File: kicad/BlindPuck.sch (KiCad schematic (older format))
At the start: 9 parts, among them Q1 FQP30N06, U1 PK-21N30P-TPQ, U2 DD06AJSA, U3 PK-21N30P-TPQ, U4 FeatherHuzzah, U5 InductiveCoil, U6 MPU-6050

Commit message: replacing the mpu6050
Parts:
- added R?: 1M, symbol R
- added R?: 100, symbol R
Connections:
- net EN(12v): now also R?.1, R?.2; no longer Q1.1 (G)
- net GND: now also U2.3 (GND(IN)), R?.2; no longer Q1.3 (S)
- net GND(12v): now also Q1.2 (D); no longer U2.2 (GND(OUT))
- new net: Q1.3 (S), U2.2 (GND(OUT))
- new net: Q1.1 (G), R?.1
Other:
- note added: "Schematic does not match PCB anymore"
- moved on the sheet: Q1
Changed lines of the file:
@@
 L GND #PWR02
 U 1 1 5A96EB1F
-P 2500 4550
-F 0 "#PWR02" H 2500 4300 50  0001 C CNN
-F 1 "GND" H 2500 4400 50  0000 C CNN
-F 2 "" H 2500 4550 50  0001 C CNN
-F 3 "" H 2500 4550 50  0001 C CNN
-	1    2500 4550
-	1    0    0    -1
-$EndComp
-Text Label 2300 2500 3    60   ~ 0
+P 2500 2500
+F 0 "#PWR02" H 2500 2250 50  0001 C CNN
+F 1 "GND" H 2500 2350 50  0000 C CNN
+F 2 "" H 2500 2500 50  0001 C CNN
+F 3 "" H 2500 2500 50  0001 C CNN
+	1    2500 2500
+	1    0    0    -1
+$EndComp
+Text Label 2250 3150 2    60   ~ 0
 GND(12v)
 Text Label 2100 2500 3    60   ~ 0
@@
 Text Label 7400 2900 0    60   ~ 0
 EN(12v)
-Text Label 1400 3750 2    60   ~ 0
+Text Label 1050 3600 2    60   ~ 0
 EN(12v)
 NoConn ~ 9200 3350
@@
 	8450 3150 9200 3150
 Wire Wire Line
-	2500 2000 2500 3550
-Wire Wire Line
-	2300 2000 2300 2500
-Wire Wire Line
 	2100 2000 2100 2500
 Wire Wire Line
@@
 Connection ~ 2500 7150
 Wire Wire Line
-	2500 3950 2500 4550
-Wire Wire Line
 	7000 1700 7300 1700
 Wire Wire Line
@@
 Wire Wire Line
 	7400 2900 7000 2900
-Wire Wire Line
-	1400 3750 2200 3750
 Wire Wire Line
 	3800 1700 4100 1700
@@
 L Q_PMOS_GDS Q1
 U 1 1 5A97569B
-P 2400 3750
-F 0 "Q1" H 2600 3800 50  0000 L CNN
-F 1 "FQP30N06" H 2600 3700 50  0000 L CNN
-F 2 "TO_SOT_Packages_THT:TO-220-3_Vertical" H 2600 3850 50  0001 C CNN
-F 3 "" H 2400 3750 50  0001 C CNN
-	1    2400 3750
+P 2150 3600
+F 0 "Q1" H 2350 3650 50  0000 L CNN
+F 1 "FQP30N06" H 2350 3550 50  0000 L CNN
+F 2 "TO_SOT_Packages_THT:TO-220-3_Vertical" H 2350 3700 50  0001 C CNN
+F 3 "" H 2150 3600 50  0001 C CNN
+	1    2150 3600
 	1    0    0    -1
 $EndComp
@@
 	1    0    0    -1
 $EndComp
+$Comp
+L GND #PWR?
+U 1 1 5AAEA265
+P 1250 4300
+F 0 "#PWR?" H 1250 4050 50  0001 C CNN
+F 1 "GND" H 1250 4150 50  0000 C CNN
+F 2 "" H 1250 4300 50  0001 C CNN
+F 3 "" H 1250 4300 50  0001 C CNN
+	1    1250 4300
+	1    0    0    -1
+$EndComp
+$Comp
+L R R?
+U 1 1 5AAEA2AF
+P 1250 3950
+F 0 "R?" V 1330 3950 50  0000 C CNN
+F 1 "1M" V 1250 3950 50  0000 C CNN
+F 2 "" V 1180 3950 50  0001 C CNN
+F 3 "" H 1250 3950 50  0001 C CNN
+	1    1250 3950
+	1    0    0    -1
+$EndComp
+$Comp
+L R R?
+U 1 1 5AAEA32B
+P 1550 3600
+F 0 "R?" V 1630 3600 50  0000 C CNN
+F 1 "100" V 1550 3600 50  0000 C CNN
+F 2 "" V 1480 3600 50  0001 C CNN
+F 3 "" H 1550 3600 50  0001 C CNN
+	1    1550 3600
+	0    1    1    0
+$EndComp
+Wire Wire Line
+	1250 4100 1250 4300
+Wire Wire Line
+	2500 2000 2500 2500
+Wire Wire Line
+	2250 3150 2250 3400
+Wire Wire Line
+	1050 3600 1400 3600
+Wire Wire Line
+	1250 3800 1250 3600
+Connection ~ 1250 3600
+Wire Wire Line
+	1700 3600 1950 3600
+Wire Wire Line
+	2250 3800 2250 3950
+Wire Wire Line
+	2250 3950 2850 3950
+Wire Wire Line
+	2850 3950 2850 2950
+Wire Wire Line
+	2850 2950 2300 2950
+Wire Wire Line
+	2300 2950 2300 2000
+Text Notes 4100 4650 0    60   ~ 0
+Schematic does not match PCB anymore
 $EndSCHEMATC

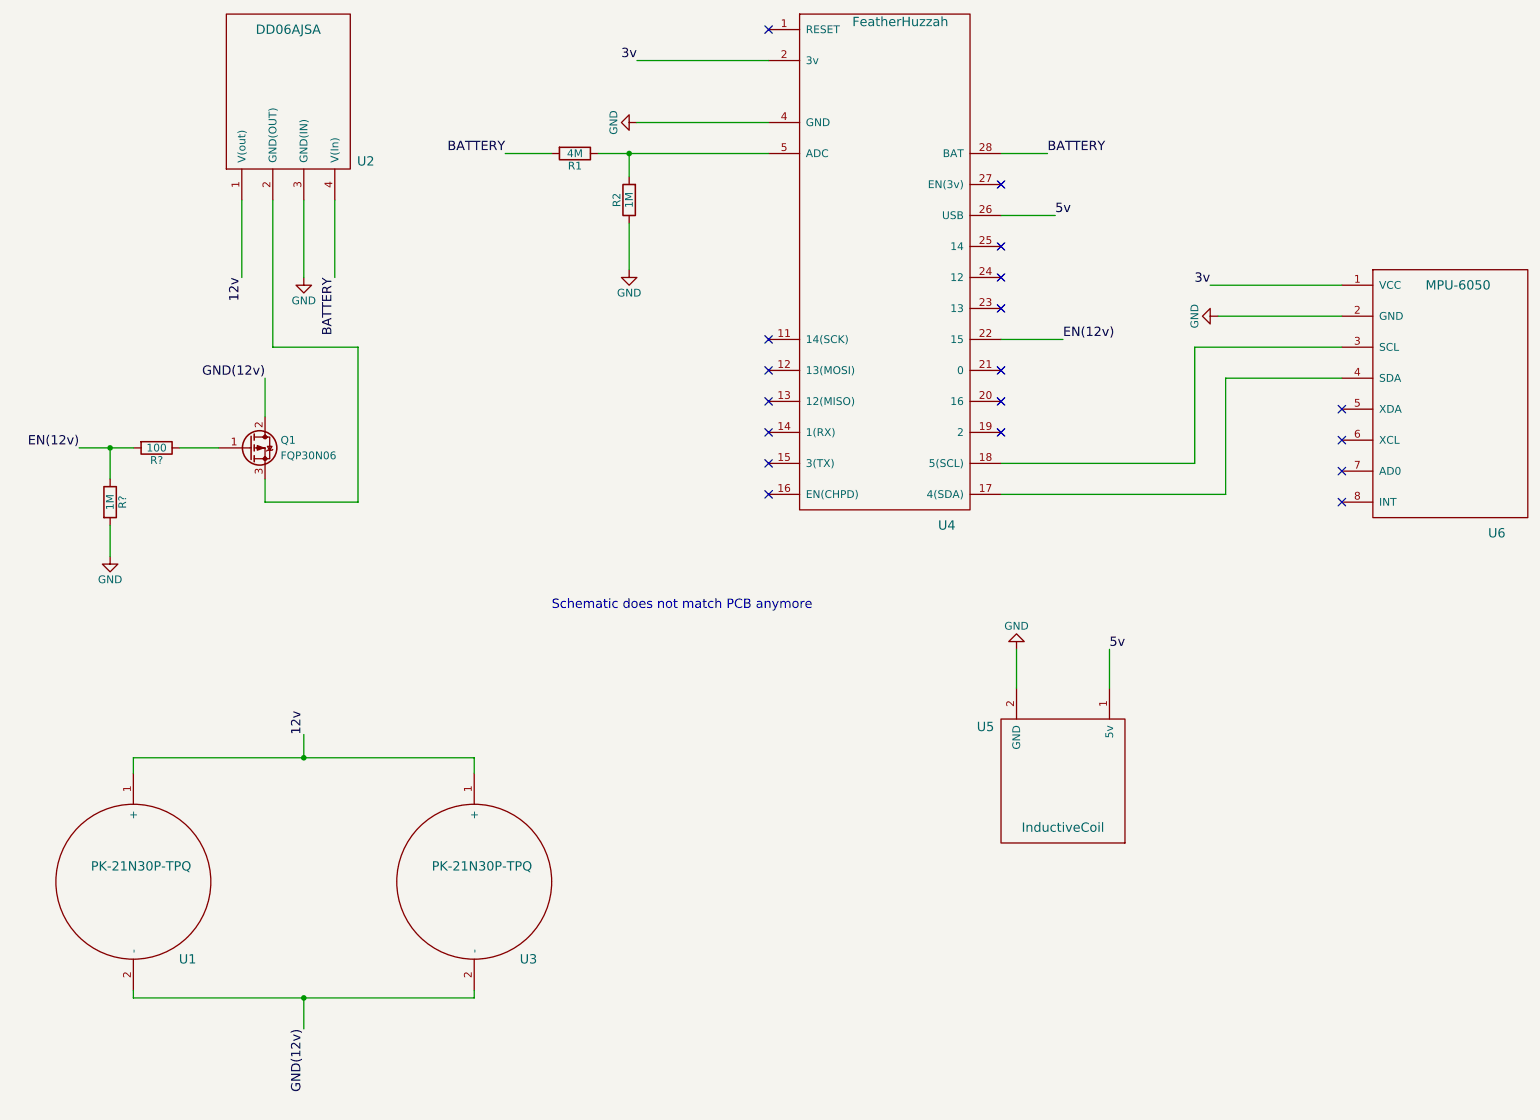
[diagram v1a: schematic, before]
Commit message: fixing Bp v3 and adding new initial work on IMS board
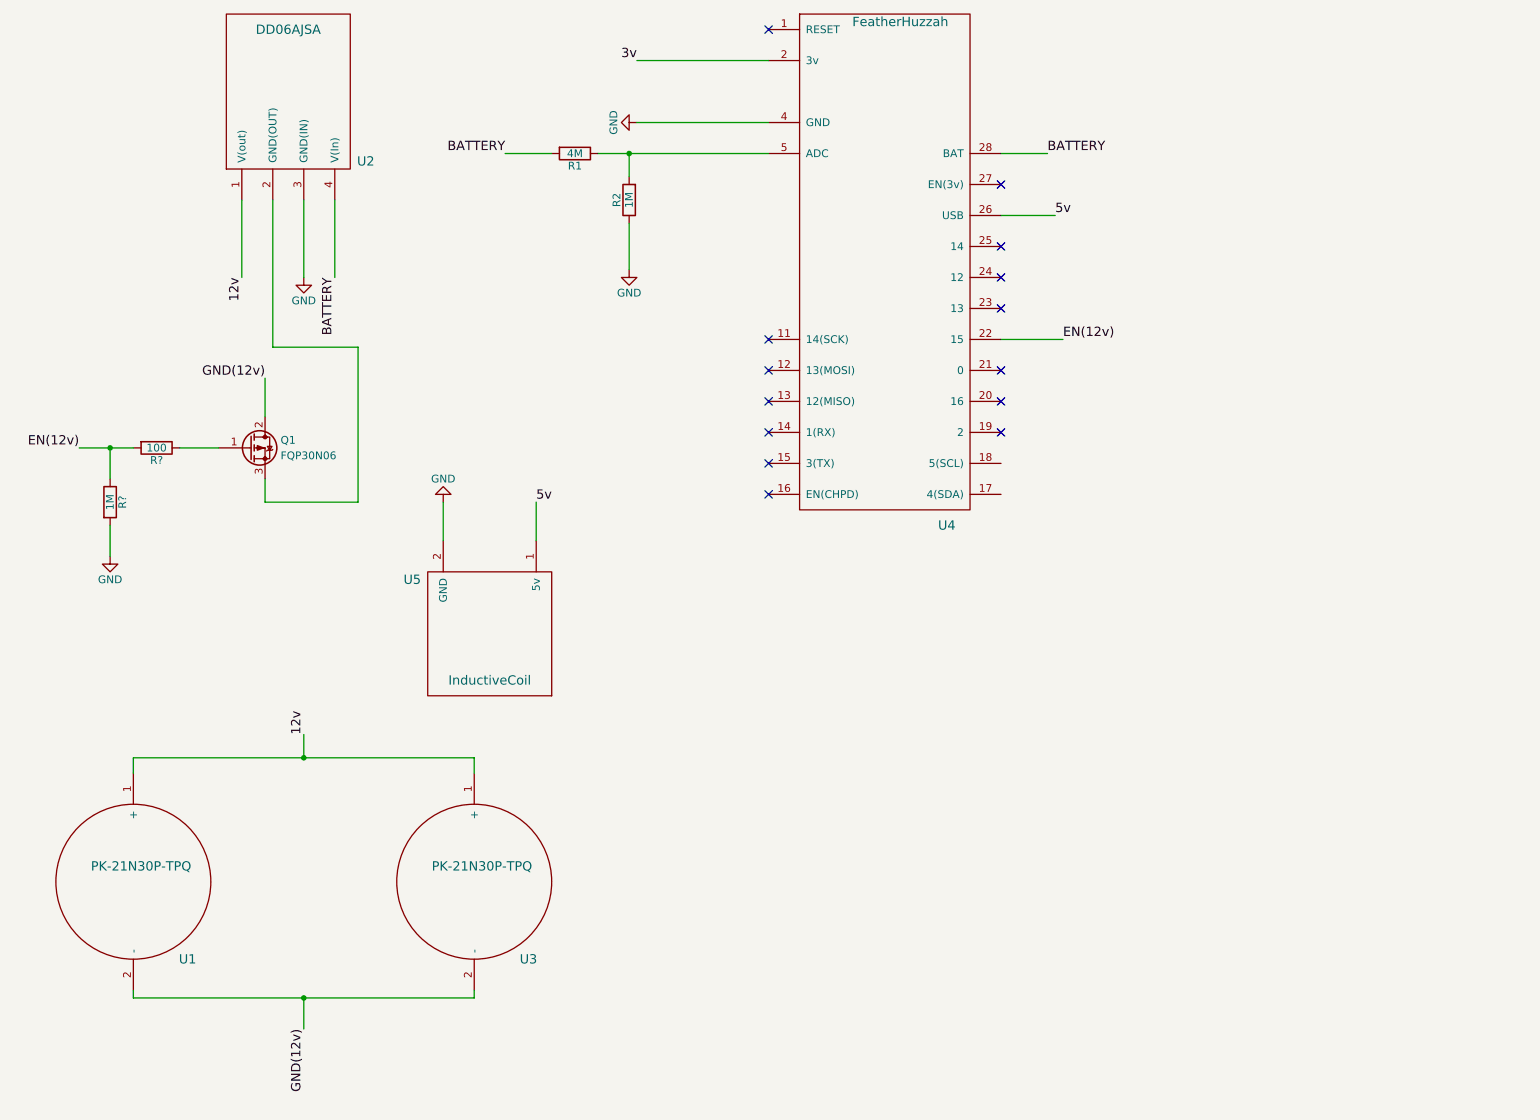
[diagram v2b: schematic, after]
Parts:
- removed U6: MPU-6050, BlindPuck:MPU6050, symbol MPU-6050-RESCUE-BlindPuck
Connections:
- no-connect marks 18 -> 14
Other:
- note removed: "Schematic does not match PCB anymore"
- moved on the sheet: U5
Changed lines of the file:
@@
-$EndComp
-$Comp
-L MPU-6050-RESCUE-BlindPuck U6
-U 1 1 5A96E8AB
-P 9800 3250
-F 0 "U6" H 10200 2350 60  0000 C CNN
-F 1 "MPU-6050" H 9950 3950 60  0000 C CNN
-F 2 "BlindPuck:MPU6050" H 9800 3250 60  0001 C CNN
-F 3 "" H 9800 3250 60  0001 C CNN
-	1    9800 3250
-	1    0    0    -1
 $EndComp
 $Comp
@@
 	1    3600 6400
 	1    0    0    -1
-$EndComp
-$Comp
-L GND #PWR01
-U 1 1 5A96EAA1
-P 8400 2750
-F 0 "#PWR01" H 8400 2500 50  0001 C CNN
-F 1 "GND" H 8400 2600 50  0000 C CNN
-F 2 "" H 8400 2750 50  0001 C CNN
-F 3 "" H 8400 2750 50  0001 C CNN
-	1    8400 2750
-	0    1    1    0
 $EndComp
 $Comp
@@
 Text Label 4650 1100 2    60   ~ 0
 3v
-Text Label 8350 2550 2    60   ~ 0
-3v
 Text Label 7400 2900 0    60   ~ 0
 EN(12v)
 Text Label 1050 3600 2    60   ~ 0
 EN(12v)
-NoConn ~ 9200 3350
-NoConn ~ 9200 3550
-NoConn ~ 9200 3750
-NoConn ~ 9200 3950
 NoConn ~ 7000 3100
 NoConn ~ 7000 3300
@@
 L GND #PWR05
 U 1 1 5A970758
-P 7100 4900
-F 0 "#PWR05" H 7100 4650 50  0001 C CNN
-F 1 "GND" H 7100 4750 50  0000 C CNN
-F 2 "" H 7100 4900 50  0001 C CNN
-F 3 "" H 7100 4900 50  0001 C CNN
-	1    7100 4900
+P 3400 3950
+F 0 "#PWR05" H 3400 3700 50  0001 C CNN
+F 1 "GND" H 3400 3800 50  0000 C CNN
+F 2 "" H 3400 3950 50  0001 C CNN
+F 3 "" H 3400 3950 50  0001 C CNN
+	1    3400 3950
 	-1   0    0    1
 $EndComp
 Text Label 7350 2100 0    60   ~ 0
 5v
-Text Label 7700 4900 0    60   ~ 0
+Text Label 4000 3950 0    60   ~ 0
 5v
 $Comp
 L InductiveCoil U5
 U 1 1 5A970AC3
-P 7400 5450
-F 0 "U5" H 7900 5400 60  0000 C CNN
-F 1 "InductiveCoil" H 7400 6050 60  0000 C CNN
-F 2 "BlindPuck:InductiveCoils(Rx)" H 7400 5450 60  0001 C CNN
-F 3 "" H 7400 5450 60  0001 C CNN
-	1    7400 5450
+P 3700 4500
+F 0 "U5" H 4200 4450 60  0000 C CNN
+F 1 "InductiveCoil" H 3700 5100 60  0000 C CNN
+F 2 "BlindPuck:InductiveCoils(Rx)" H 3700 4500 60  0001 C CNN
+F 3 "" H 3700 4500 60  0001 C CNN
+	1    3700 4500
 	-1   0    0    1
 $EndComp
-Wire Wire Line
-	9200 2950 8250 2950
-Wire Wire Line
-	8250 2950 8250 3700
-Wire Wire Line
-	8250 3700 7000 3700
-Wire Wire Line
-	7000 3900 8450 3900
-Wire Wire Line
-	8450 3900 8450 3150
-Wire Wire Line
-	8450 3150 9200 3150
 Wire Wire Line
 	2100 2000 2100 2500
@@
 	4650 1500 5500 1500
 Wire Wire Line
-	8400 2750 9200 2750
-Wire Wire Line
 	5500 1100 4650 1100
-Wire Wire Line
-	8350 2550 9200 2550
 Wire Wire Line
 	7400 2900 7000 2900
@@
 	7350 2100 7000 2100
 Wire Wire Line
-	7100 4900 7100 5150
-Wire Wire Line
-	7700 4900 7700 5150
+	3400 3950 3400 4200
+Wire Wire Line
+	4000 3950 4000 4200
 $Comp
 L Q_PMOS_GDS Q1
@@
 Wire Wire Line
 	2300 2950 2300 2000
-Text Notes 4100 4650 0    60   ~ 0
-Schematic does not match PCB anymore
 $EndSCHEMATC
